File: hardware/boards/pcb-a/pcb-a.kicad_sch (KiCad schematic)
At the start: 37 parts, among them J1 to carrier J5 (IDC 2x15), J2 I2C in (JST-SH 4, Qwiic), J3 to PCB-F (JST-SH 6), J4 to PCB-K1 (JST-SH 10), U1 MCP23017-E/SO

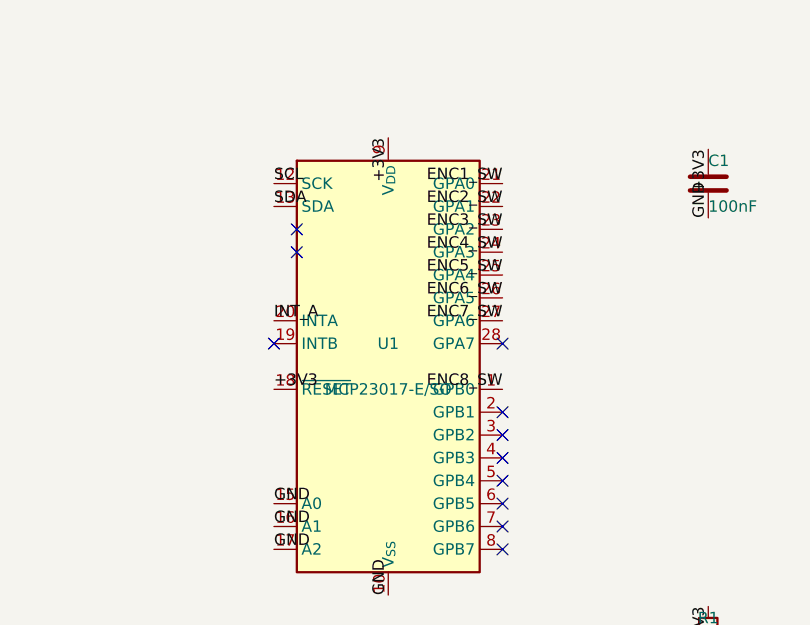
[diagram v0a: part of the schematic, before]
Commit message: hw(boards): all panel boards routed to DRC 0/0/0, add PCB-S shield adapter, fab outputs
PCB-A, PCB-F, PCB-K1, PCB-K2 and the new PCB-S pass DRC with schematic parity and ERC.
Single-sided bottom assembly; PCB-S ships bare (hand-soldered).

- PCB-A: MCP23017 0x20 moved to SSOP-28 in the front band between E4 and E5; J4 (to PCB-K1)
  moved to the tab next to J1 (cable ~20-25 cm) so the bus stays off the encoder strip;
  strip front edge 99 -> 97.5; H4 onto the tab.
- PCB-K1: MCP 0x21 pins reordered for a planar fan-out; U1 is SSOP-28; J2 over U2.
- PCB-S: shield adapter for the carrier's J15/J16 (I2C -> JST-SH 4, Serial5 -> JST-PH 4 to the M4).
- tools: grid router now sees footprint Edge.Cuts windows and exact pad keep-outs; finish_routing
  routes shortest-first, joins split nets and rips up endpoint blockers; new repair_routes.py and
  tie_loose_gnd.py; GND escapes respect the real outline; sync_from_netlist re-assigns pad nets;
  export_fab groups BOM lines per part and covers PCB-S.
- fab/: Gerbers, BOM and CPL per board for JLCPCB.

Co-Authored-By: Claude Sonnet 5.5 <noreply@anthropic.com>
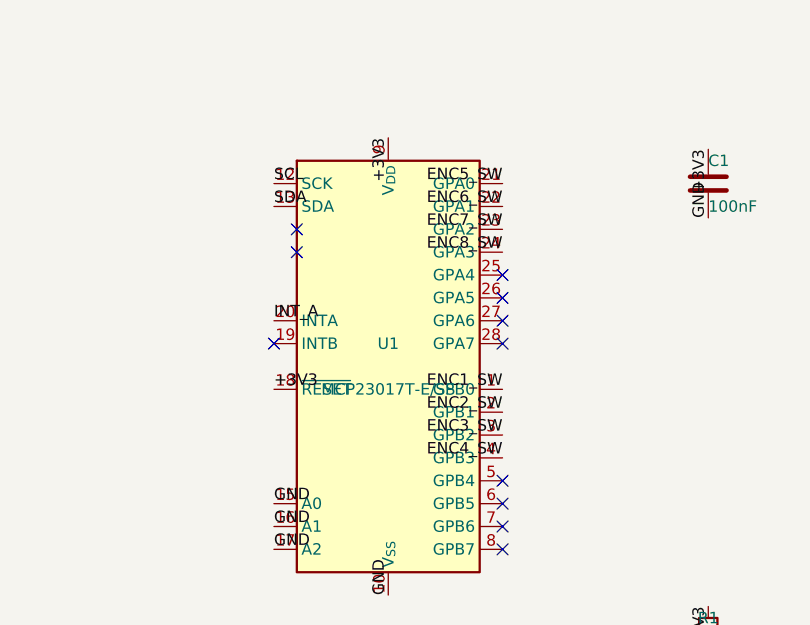
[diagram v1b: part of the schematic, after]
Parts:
- C1: LCSC (none) -> C14663
- C10, C11, C12, C13, C14, C15, C16, C17, C18, C19, C20, C21, C22, C23, C24, C25: LCSC (none) -> C57112
- C2: LCSC (none) -> C15850
- J2: LCSC (none) -> C160404
- J3: LCSC (none) -> C160405
- J4: LCSC (none) -> C160409
- R1, R2: LCSC (none) -> C23162
- U1: value MCP23017-E/SO -> MCP23017T-E/SS; footprint Package_SO:SOIC-28W_7.5x17.9mm_P1.27mm -> Package_SO:SSOP-28_5.3x10.2mm_P0.65mm; LCSC (none) -> C558584
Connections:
- net ENC1_SW: now also U1.1 (GPB0); no longer U1.21 (GPA0)
- net ENC2_SW: now also U1.2 (GPB1); no longer U1.22 (GPA1)
- net ENC3_SW: now also U1.3 (GPB2); no longer U1.23 (GPA2)
- net ENC4_SW: now also U1.4 (GPB3); no longer U1.24 (GPA3)
- net ENC5_SW: now also U1.21 (GPA0); no longer U1.25 (GPA4)
- net ENC6_SW: now also U1.22 (GPA1); no longer U1.26 (GPA5)
- net ENC7_SW: now also U1.23 (GPA2); no longer U1.27 (GPA6)
- net ENC8_SW: now also U1.24 (GPA3); no longer U1.1 (GPB0)
